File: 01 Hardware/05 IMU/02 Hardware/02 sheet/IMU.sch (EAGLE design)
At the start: 1 part, among them U2 RASPBERRY_PICOTH

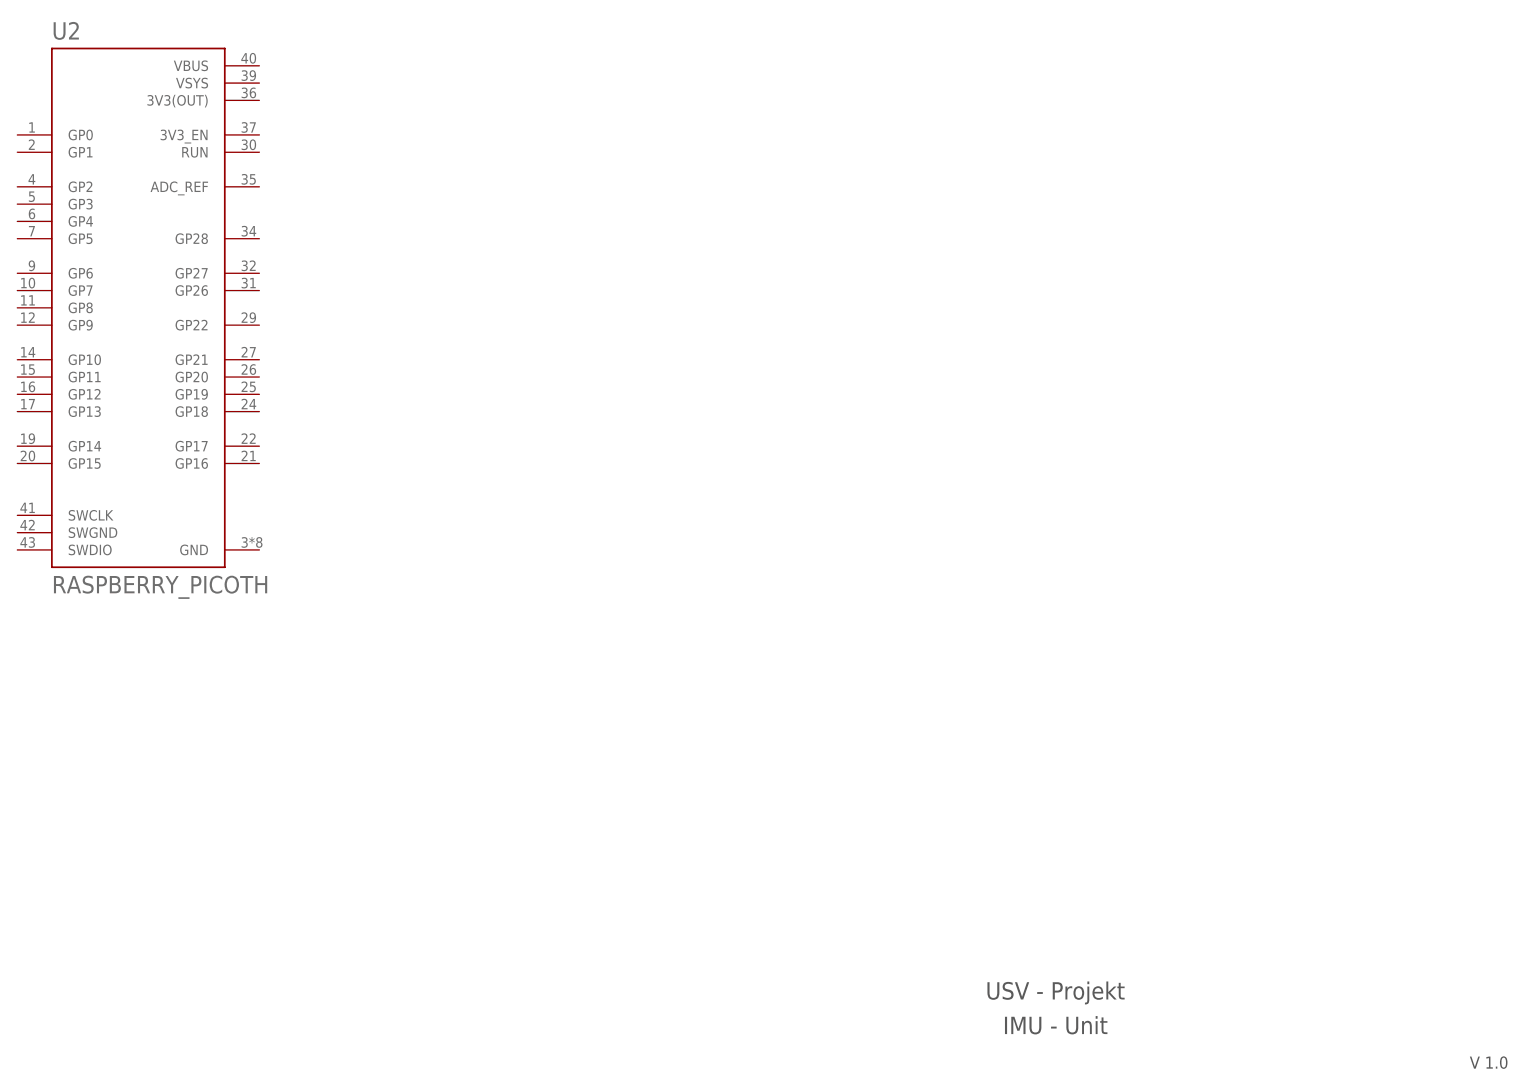
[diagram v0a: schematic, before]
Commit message: USV Slave Template
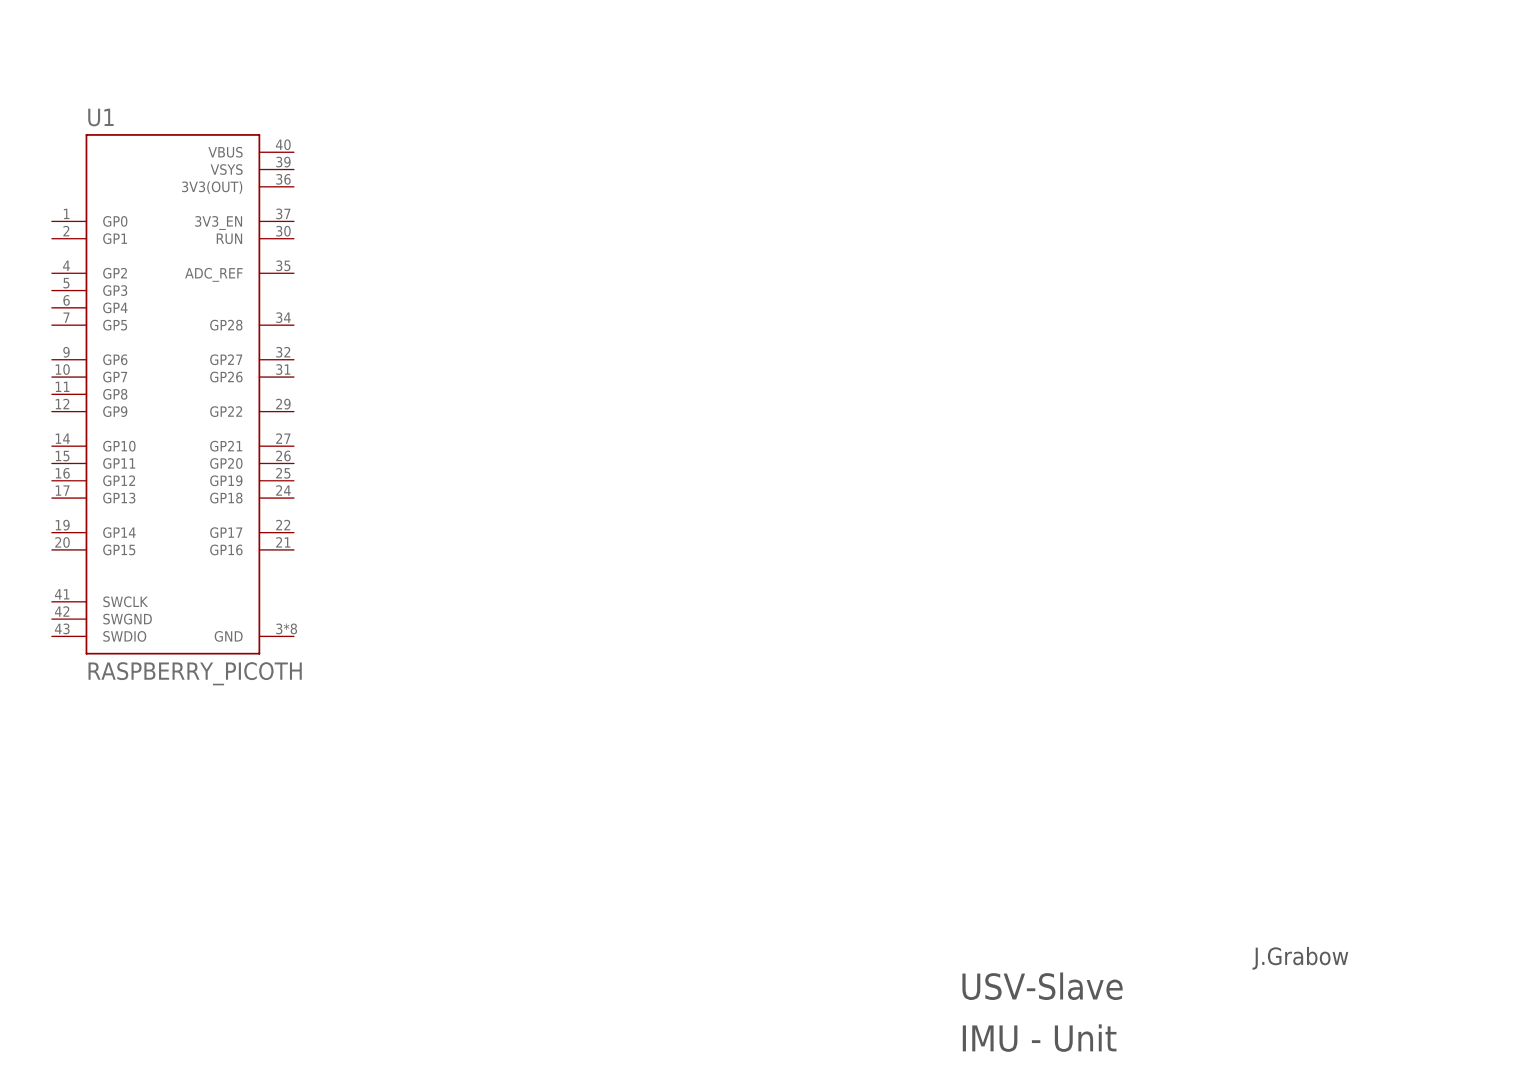
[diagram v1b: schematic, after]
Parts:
- removed U2: RASPBERRY_PICOTH, RpiPico:RASPBERRY_PICOTH
- added U1: RASPBERRY_PICOTH, RpiPico:RASPBERRY_PICOTH
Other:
- note added: "J.Grabow"
- note added: "USV-Slave"
- note removed: "USV - Projekt"
- note removed: "V 1.0"
